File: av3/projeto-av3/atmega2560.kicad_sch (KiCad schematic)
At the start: 4 parts, among them U5 ATmega2560-16A, Y1 16MHz

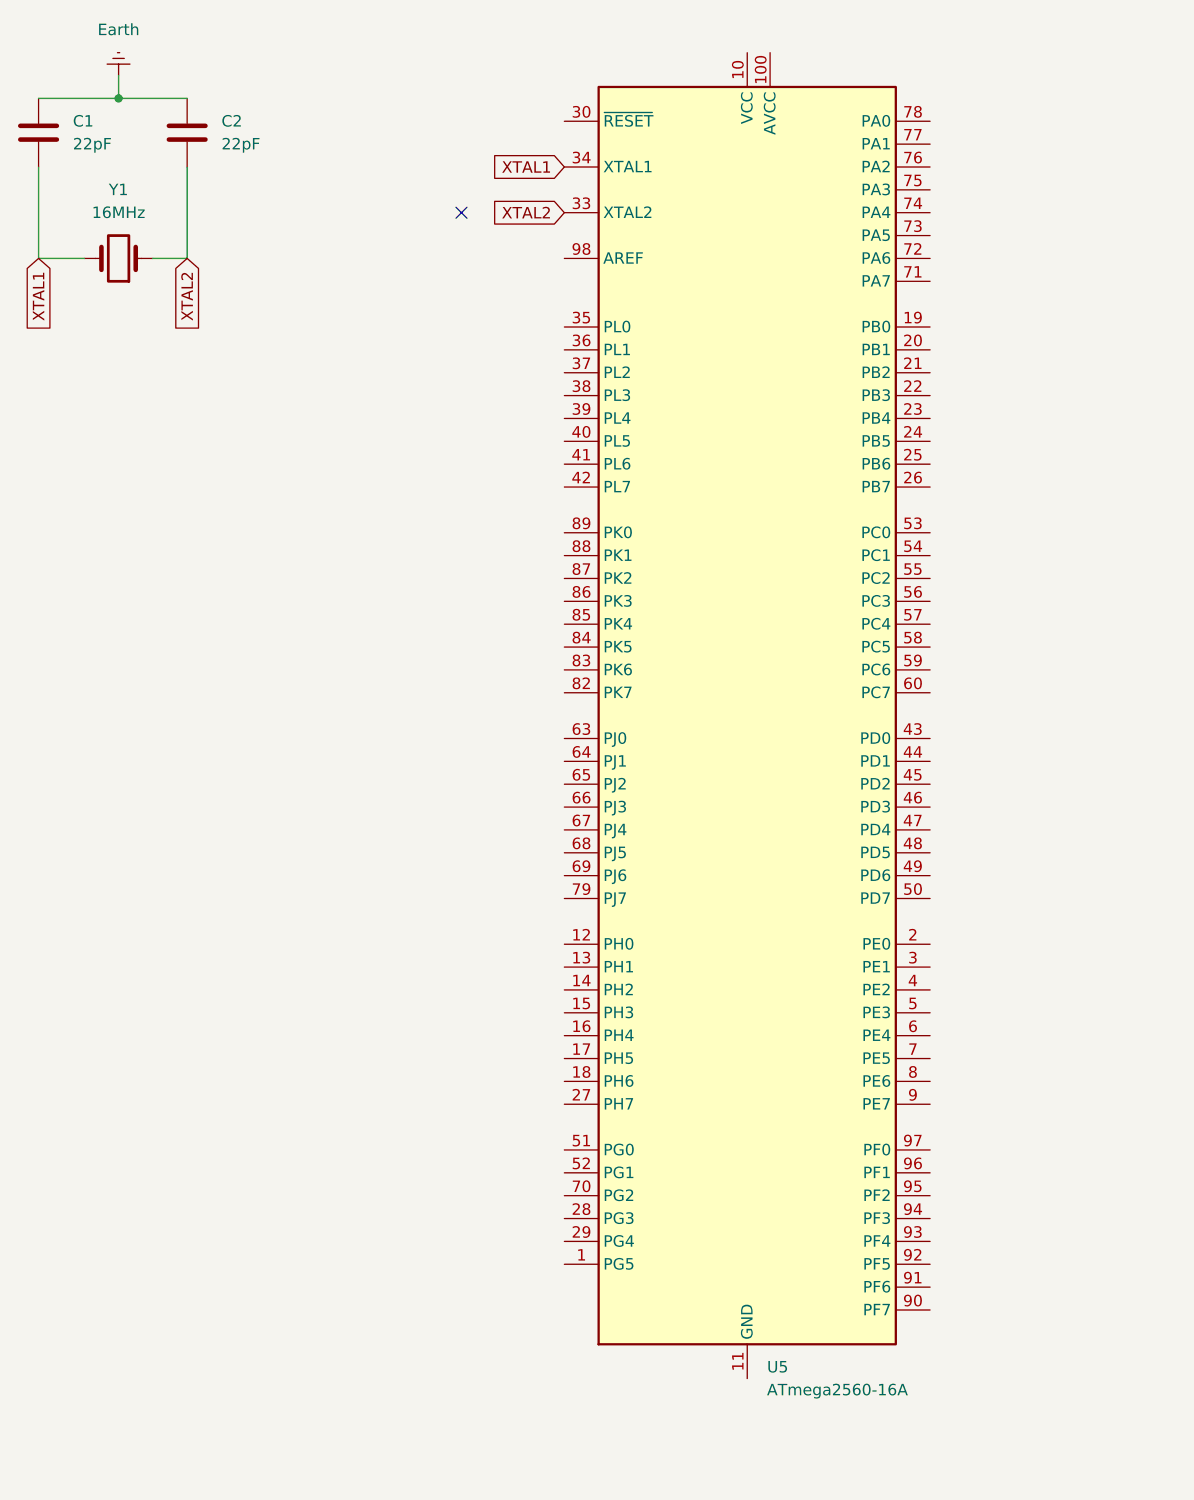
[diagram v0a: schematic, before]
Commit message: Maioria dos esquemáticos finalizados.
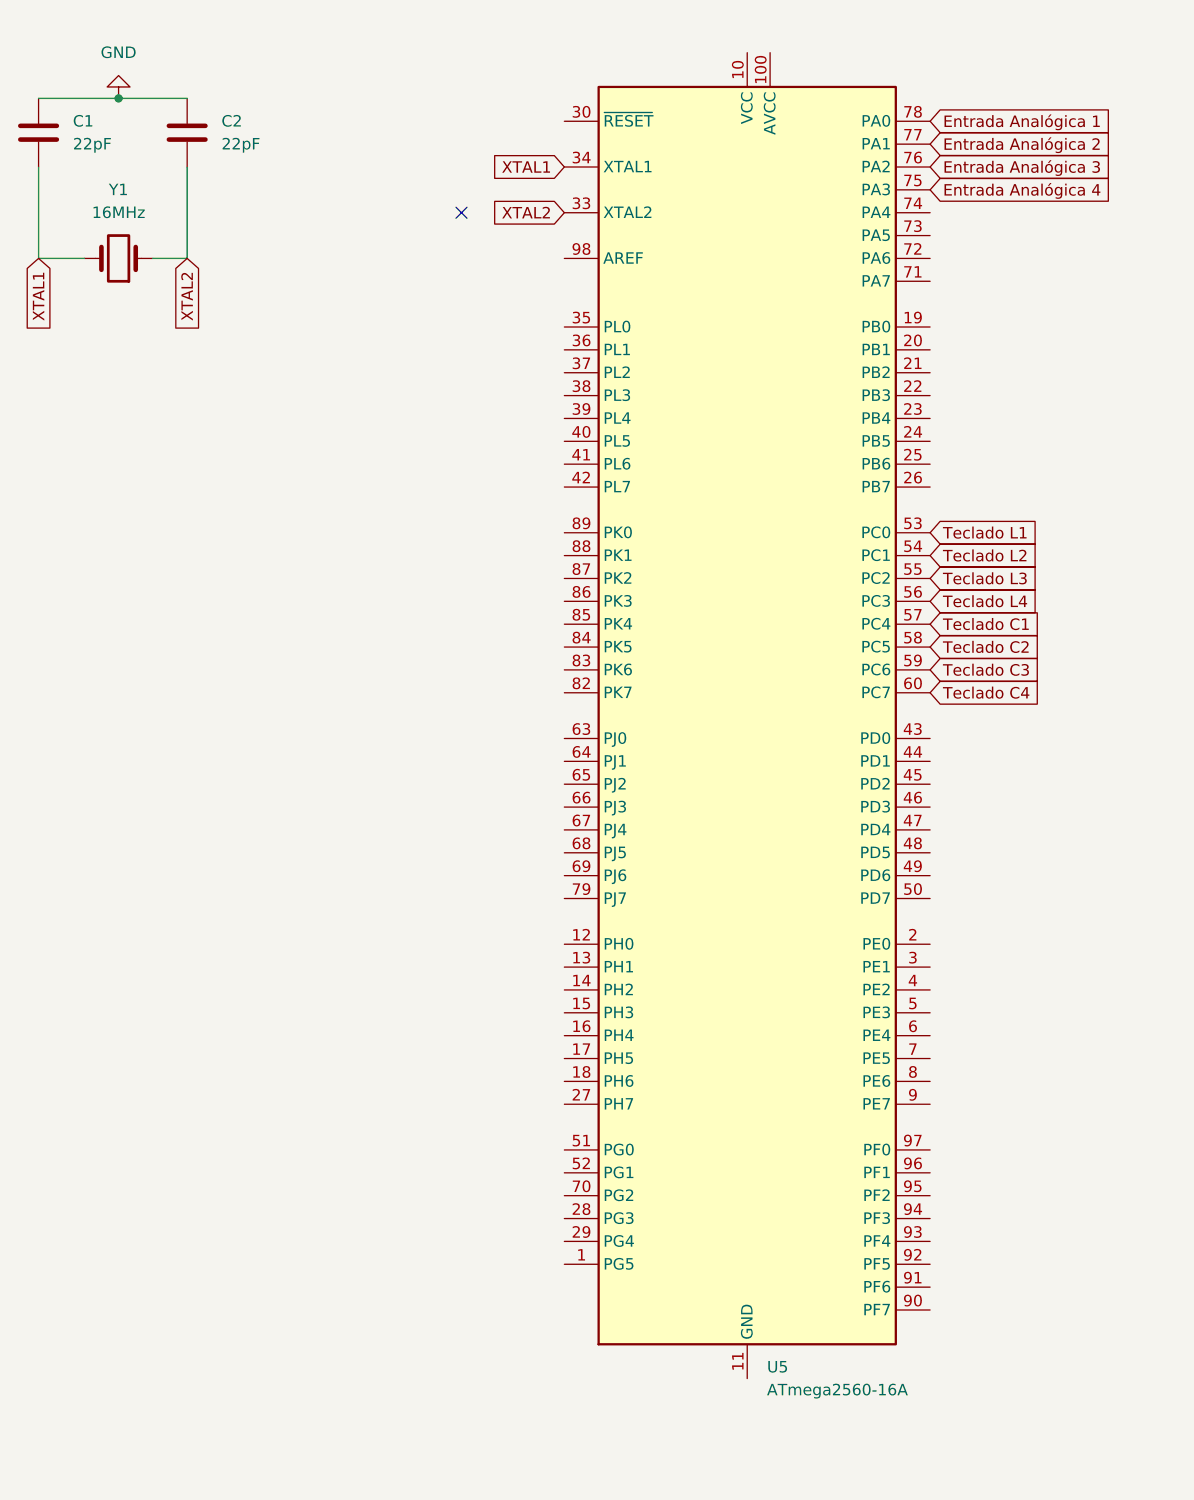
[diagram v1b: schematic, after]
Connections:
- net Teclado L1: now reaches U5.53 (PC0)
- net Teclado L2: now reaches U5.54 (PC1)
- net Teclado L3: now reaches U5.55 (PC2)
- net Teclado L4: now reaches U5.56 (PC3)
- net Teclado C1: now reaches U5.57 (PC4)
- net Teclado C2: now reaches U5.58 (PC5)
- net Teclado C3: now reaches U5.59 (PC6)
- net Teclado C4: now reaches U5.60 (PC7)
- net Entrada Analógica 4: now reaches U5.75 (PA3)
- net Entrada Analógica 3: now reaches U5.76 (PA2)
- net Entrada Analógica 2: now reaches U5.77 (PA1)
- net Entrada Analógica 1: now reaches U5.78 (PA0)
- net Earth renamed GND

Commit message: Esquemático finalizado, faltando somente o PCB.
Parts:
- removed C1, C2: 22pF, symbol Device:C
- removed Y1: 16MHz, symbol Device:Crystal
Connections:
- net GND: now also U5.11 (GND), U5.32 (GND), U5.62 (GND), U5.81 (GND), U5.99 (GND)
- net I.0: now reaches U5.12 (PH0)
- net I.1: now reaches U5.13 (PH1)
- net I.2: now reaches U5.14 (PH2)
- net I.3: now reaches U5.15 (PH3)
- net I.4: now reaches U5.16 (PH4)
- net I.5: now reaches U5.17 (PH5)
- net I.6: now reaches U5.18 (PH6)
- net RX: now reaches U5.2 (PE0)
- net SCK: now reaches U5.20 (PB1)
- net MOSI: now reaches U5.21 (PB2)
- net MISO: now reaches U5.22 (PB3)
- net I.7: now reaches U5.27 (PH7)
- net TX: now reaches U5.3 (PE1)
- net reset: now reaches U5.30 (~{RESET})
- net O.0: now reaches U5.35 (PL0)
- net O.1: now reaches U5.36 (PL1)
- net O.2: now reaches U5.37 (PL2)
- net O.3: now reaches U5.38 (PL3)
- net O.4: now reaches U5.39 (PL4)
- net O.5: now reaches U5.40 (PL5)
- net O.6: now reaches U5.41 (PL6)
- net O.7: now reaches U5.42 (PL7)
- net RS: now reaches U5.63 (PJ0)
- net E: now reaches U5.64 (PJ1)
- net D7: now reaches U5.71 (PA7)
- net D6: now reaches U5.72 (PA6)
- net D5: now reaches U5.73 (PA5)
- net D4: now reaches U5.74 (PA4)
- net L4: now reaches U5.82 (PK7)
- net L3: now reaches U5.83 (PK6)
- net L2: now reaches U5.84 (PK5)
- net L1: now reaches U5.85 (PK4)
- net C4: now reaches U5.86 (PK3)
- net C3: now reaches U5.87 (PK2)
- net C2: now reaches U5.88 (PK1)
- net C1: now reaches U5.89 (PK0)
- net ADC7: now reaches U5.90 (PF7)
- net ADC6: now reaches U5.91 (PF6)
- net ADC5: now reaches U5.92 (PF5)
- net ADC4: now reaches U5.93 (PF4)
- net ADC3: now reaches U5.94 (PF3)
- net ADC2: now reaches U5.95 (PF2)
- net ADC1: now reaches U5.96 (PF1)
- net ADC0: now reaches U5.97 (PF0)
- net +5V: now reaches U5.98 (AREF)
- net Entrada Analógica 1: no longer names the net of U5.78 (PA0)
- net Entrada Analógica 2: no longer names the net of U5.77 (PA1)
- net Entrada Analógica 3: no longer names the net of U5.76 (PA2)
- net Entrada Analógica 4: no longer names the net of U5.75 (PA3)
- net Teclado C1: no longer names the net of U5.57 (PC4)
- net Teclado C2: no longer names the net of U5.58 (PC5)
- net Teclado C3: no longer names the net of U5.59 (PC6)
- net Teclado C4: no longer names the net of U5.60 (PC7)
- net Teclado L1: no longer names the net of U5.53 (PC0)
- net Teclado L2: no longer names the net of U5.54 (PC1)
- net Teclado L3: no longer names the net of U5.55 (PC2)
- net Teclado L4: no longer names the net of U5.56 (PC3)
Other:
- moved on the sheet: U5

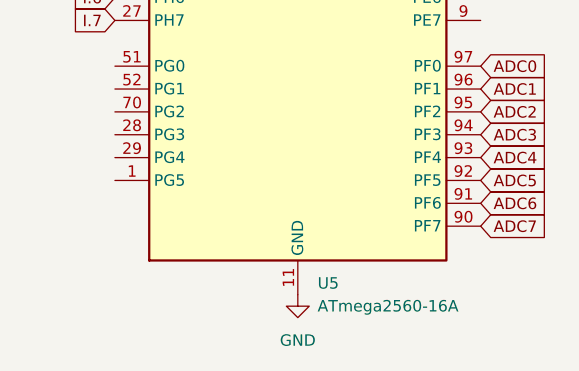
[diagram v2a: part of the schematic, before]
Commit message: Referencias de componentes resetados; Progresso de 20% no PCB;
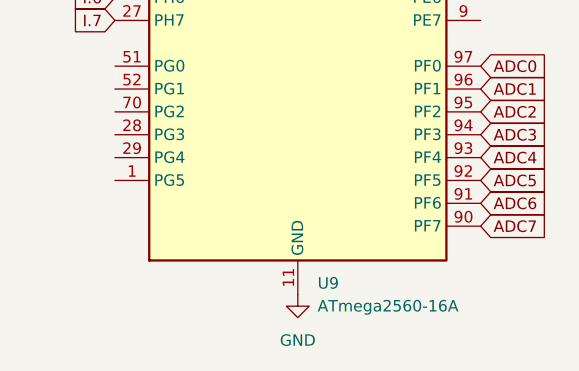
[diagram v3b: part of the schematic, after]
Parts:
- renumbered U5 to U9
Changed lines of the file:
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@@
 		(dnp no)
 		(fields_autoplaced yes)
-		(property "Reference" "#PWR065"
+		(property "Reference" "#PWR052"
 			(at 91.44 53.34 0)
 			(effects
@@
 			(project "av3"
 				(path "/82998b71-606c-4e03-99b7-477e2a65cb94/a11288ef-de27-492e-b20f-7cae37fe8404"
-					(reference "#PWR065")
+					(reference "#PWR052")
 					(unit 1)
 				)
@@
 		(dnp no)
 		(fields_autoplaced yes)
-		(property "Reference" "U5"
+		(property "Reference" "U9"
 			(at 110.1441 176.53 0)
 			(effects
@@
 			(project "av3"
 				(path "/82998b71-606c-4e03-99b7-477e2a65cb94/a11288ef-de27-492e-b20f-7cae37fe8404"
-					(reference "U5")
+					(reference "U9")
 					(unit 1)
 				)
@@
 		(dnp no)
 		(fields_autoplaced yes)
-		(property "Reference" "#PWR066"
+		(property "Reference" "#PWR053"
 			(at 107.95 184.15 0)
 			(effects
@@
 			(project "av3"
 				(path "/82998b71-606c-4e03-99b7-477e2a65cb94/a11288ef-de27-492e-b20f-7cae37fe8404"
-					(reference "#PWR066")
+					(reference "#PWR053")
 					(unit 1)
 				)
